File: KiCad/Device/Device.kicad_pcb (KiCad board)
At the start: 2 copper layers, 53.5 x 64 mm, 25 parts, among them IC1 ATTINY167-XUR, J5 VCC, J6 ESP8266(wifi), J7 Conn_02x06_Counter_Clockwise, SW1 SW_MEC_5E, SW3 SW_MEC_5E, SW4 SW_DIP_x02, Y1 Crystal

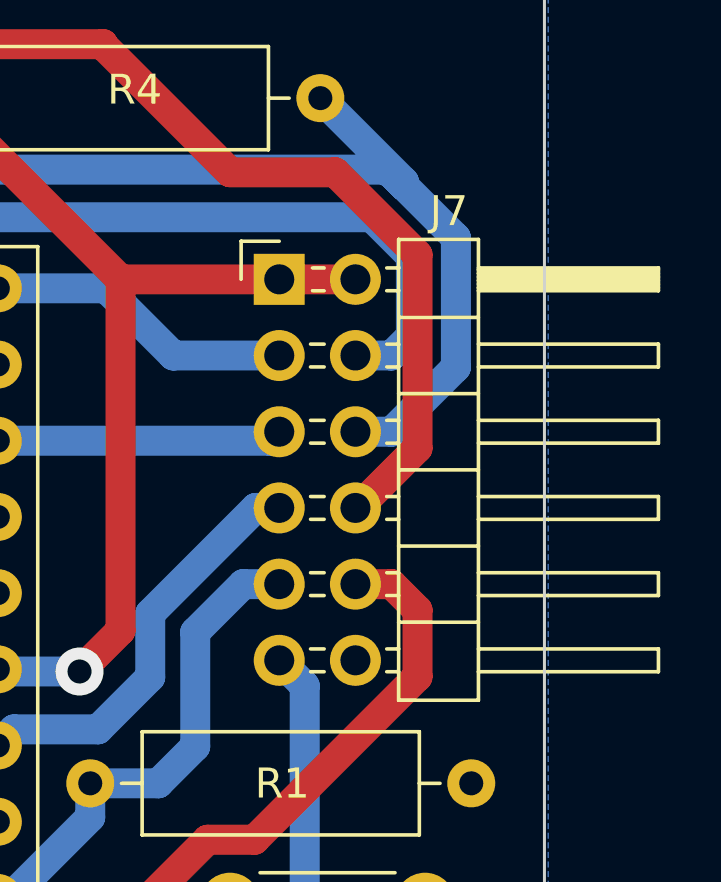
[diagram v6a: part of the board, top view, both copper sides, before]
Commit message: Opdateret connecter 5v
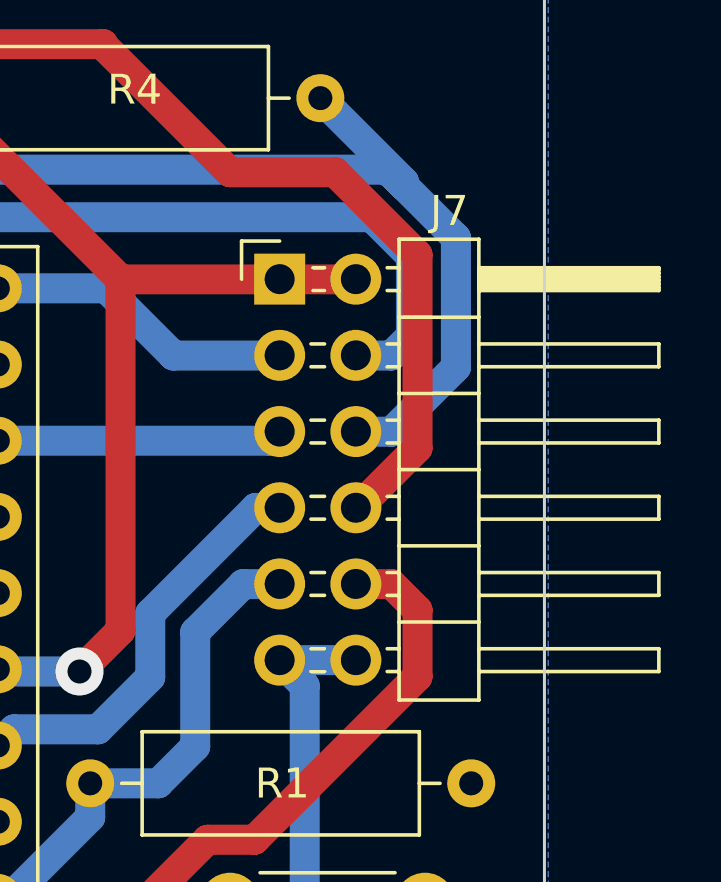
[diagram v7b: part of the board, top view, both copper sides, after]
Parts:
- J7: value Conn_02x06_Counter_Clockwise -> Conn_02x06_Odd_Even
- R1: value 10k -> 2k
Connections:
- J7 pad 12: UPWR -> +5V
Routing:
- net +5V: track 132.3 -> 134.8 mm

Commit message: kicad
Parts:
- removed C1: 1uF, Capacitor_THT:C_Disc_D5.0mm_W2.5mm_P5.00mm
- removed R2: 2.2k, Resistor_THT:R_Axial_DIN0309_L9.0mm_D3.2mm_P12.70mm_Horizontal
- C4: value 200n -> 100pF
- moved D3 19.0 mm to (77.7, 66.0)
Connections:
- D3 pad 1: +3V3 -> +5V
- IC1 pad 11: UP7 -> MIC
- J7 pad 10: UP7 -> MIC
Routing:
- net UP7: track 31.6 -> 0.00 mm
- net MIC: track 11.6 -> 23.4 mm, vias 0 -> 1
- net +5V: track 134.8 -> 129.2 mm
- net Button01: track 53.5 -> 49.6 mm
